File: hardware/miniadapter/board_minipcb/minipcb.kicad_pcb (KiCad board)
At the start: 2 copper layers, 8.5 x 12.7 mm, 22 parts, among them Q102 FDG1024NZ, U102 SN74LVC1G14DRL, U103 TPS62933P

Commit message: new layout
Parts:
- added H108: Pad, Connector_Wire:SolderWirePad_1x01_SMD_1.5x3mm, F.Cu at (107.1, 101.1)
- added H109: Pad, Connector_Wire:SolderWirePad_1x01_SMD_1.5x3mm, F.Cu at (102.0, 101.1)
- added H110: Pad, Connector_Wire:SolderWirePad_1x01_SMD_1.5x3mm, F.Cu at (103.3, 101.1)
- added H111: Pad, Connector_Wire:SolderWirePad_1x01_SMD_1.5x3mm, F.Cu at (100.7, 101.1)
- added REF**: Tab, PCM_kikit:Tab, F.Cu at (104.2, 112.7)
- added REF**: Tab, PCM_kikit:Tab, F.Cu at (108.5, 110.0)
- added REF**: Tab, PCM_kikit:Tab, F.Cu at (100.0, 102.0)
- C101, R103: moved to B.Cu
- C102, R101, R105: moved to F.Cu
- H101, H102, H103, H104, H105, H106, H107: value MountingHole_Pad -> Pad
- moved C103 5.63 mm to (101.0, 104.1), turned to 180 degrees
- moved R103 5.44 mm to (100.8, 107.4), turned to 90 degrees
- moved H101 5.00 mm to (101.8, 110.8)
- moved H103 5.00 mm to (106.8, 110.8)
- moved D101 4.90 mm to (101.2, 106.3), turned to -90 degrees
- moved C101 4.54 mm to (103.0, 108.1), turned to 180 degrees
- moved R105 3.40 mm to (103.3, 103.1)
- moved U102 3.33 mm to (101.0, 104.1)
- moved R101 2.41 mm to (106.8, 106.9)
- moved C102 2.30 mm to (106.2, 103.9), turned to 180 degrees
- moved R102 2.15 mm to (102.0, 106.5), turned to 90 degrees
- moved Q102 1.86 mm to (103.3, 103.9)
- moved R106 0.71 mm to (102.9, 106.5), turned to 90 degrees
- moved R104 0.57 mm to (104.2, 106.5)
- moved C104 0.30 mm to (105.2, 107.2)
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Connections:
- H104 pad 1: +3V3 -> /IO4
- H105 pad 1: /IO4 -> /IO5
- H106 pad 1: GND -> +3V3
- H107 pad 1: /IO5 -> GND
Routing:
- net /IO4: track 7.79 -> 3.32 mm, vias 0 -> 1
- net /DBUS: track 3.73 -> 8.09 mm, vias 1 -> 0
- net /DBUS_R: track 10.2 -> 6.22 mm
- net GND: track 8.01 -> 4.10 mm, vias 11 -> 8
- net /V-: track 9.38 -> 13.1 mm
- net /IO5: track 5.86 -> 3.34 mm, vias 0 -> 1
- net +3V3: track 12.4 -> 10.5 mm, vias 0 -> 4
- net /V+: track 10.2 -> 8.75 mm
- net /SW: track 1.07 -> 2.40 mm
- net /FB: track 4.83 -> 6.01 mm, vias 0 -> 1
- net /IN: track 3.79 -> 4.73 mm
- added copper zone on B.Cu, net +3V3
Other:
- board text added: "3V3"
- board text added: "GND"
- board text added: "IO4"
- board text added: "IO5"

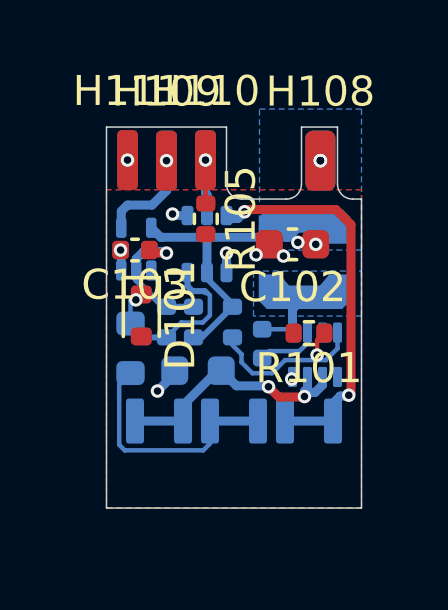
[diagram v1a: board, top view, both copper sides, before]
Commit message: layout changes and panel generation
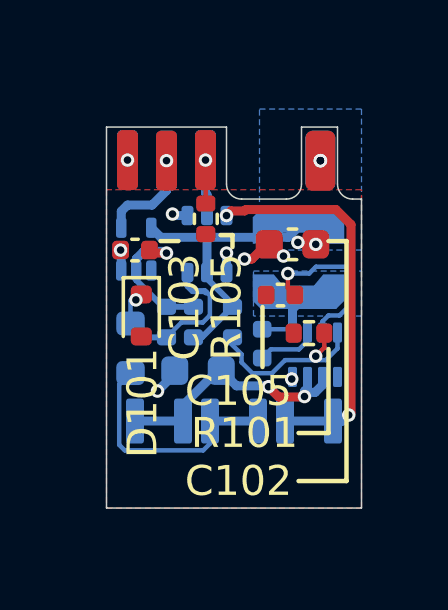
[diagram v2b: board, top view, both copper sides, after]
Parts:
- added C105: C_100n_0402_X7R_10%_50V, Capacitor_SMD:C_0402_1005Metric, F.Cu at (105.8, 105.6)
- L101: value SRN3015C-2R2M -> FTC252075S
- Q102: value FDG1024NZ -> FDG1024NZ-VB
- R101: value R_24K0_0402_0W063_1%_100PPM_50V -> R_15K_0402_0W063_1%_100PPM_50V
- R104, R105, R106: value R_75K_0402_0W063_1%_100PPM_50V -> R_47K_0402_0W063_1%_100PPM_50V
- U103: value TPS62933P -> TPS62933DRLR
- moved REF** 1.10 mm to (108.5, 111.1)
- moved REF** 0.40 mm to (100.0, 101.6)
- moved L101 0.20 mm to (106.4, 104.4)
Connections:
- U103 pad 7: unconnected-(U103-PG-Pad7) -> Net-(U103-SS)
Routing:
- net Net-(U103-SS): track 0.00 -> 5.73 mm, vias 0 -> 1

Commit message: top layer changes minipcb
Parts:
- moved R105 2.53 mm to (100.8, 103.4), turned to 180 degrees
- moved C105 1.97 mm to (107.5, 106.6), turned to -90 degrees
- moved R101 1.94 mm to (107.4, 108.7), turned to -90 degrees
- moved C102 1.21 mm to (107.3, 104.3), turned to -90 degrees
- moved C103 0.80 mm to (100.9, 104.9)
- moved D101 0.49 mm to (100.9, 106.7)
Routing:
- net /IO4: track 3.32 -> 5.89 mm, vias 1 -> 2
- net GND: track 4.55 -> 2.86 mm
- net Net-(U103-SS): track 5.73 -> 7.17 mm
